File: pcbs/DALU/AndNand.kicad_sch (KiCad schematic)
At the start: 2 parts, among them U301 74HC00, U302 74HC00

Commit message: Trying to figure out the hierarchical buses
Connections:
- net NAND1: now reaches U301.6
- net RESULT0 renamed NAND0
- net RESULT2 renamed NAND2
- net RESULT3 renamed NAND3
- net RESULT4 renamed NAND4
- net RESULT5 renamed NAND5
- net RESULT6 renamed NAND6
- net RESULT7 renamed NAND7

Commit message: Trying to get everything together
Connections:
- net +5V: now reaches U302.14 (VCC)
- net +5V: now also U301.14 (VCC)
- net GND: now reaches U302.7 (GND)
- net GND: now also U301.7 (GND)
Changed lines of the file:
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@@
+    (stroke (width 0) (type default) (color 0 0 0 0))
+  )
+  (wire (pts (xy 25.4 190.5) (xy 25.4 193.04))
     (stroke (width 0) (type default) (color 0 0 0 0))
   )
@@
     (stroke (width 0) (type default) (color 0 0 0 0))
   )
+  (wire (pts (xy 25.4 162.56) (xy 25.4 165.1))
+    (stroke (width 0) (type default) (color 0 0 0 0))
+  )
   (bus (pts (xy 114.3 110.49) (xy 114.3 124.46))
     (stroke (width 0) (type default) (color 0 0 0 0))
@@
     (stroke (width 0) (type default) (color 0 0 0 0))
   )
+  (wire (pts (xy 53.34 190.5) (xy 53.34 193.04))
+    (stroke (width 0) (type default) (color 0 0 0 0))
+  )
   (bus (pts (xy 120.65 27.94) (xy 114.3 27.94))
     (stroke (width 0) (type default) (color 0 0 0 0))
@@
   )
   (bus (pts (xy 60.96 93.98) (xy 60.96 107.95))
+    (stroke (width 0) (type default) (color 0 0 0 0))
+  )
+  (wire (pts (xy 53.34 162.56) (xy 53.34 165.1))
     (stroke (width 0) (type default) (color 0 0 0 0))
   )
@@
   (hierarchical_label "A[0..7]" (shape input) (at 24.13 25.4 180)
     (effects (font (size 1.27 1.27)) (justify right))
+  )
+  (symbol (lib_id "power:+5V") (at 53.34 162.56 0) (unit 1)
+    (in_bom yes) (on_board yes) (fields_autoplaced)
+    (property "Reference" "#PWR0303" (id 0) (at 53.34 166.37 0)
+      (effects (font (size 1.27 1.27)) hide)
+    )
+    (property "Value" "+5V" (id 1) (at 53.34 157.48 0))
+    (property "Footprint" "" (id 2) (at 53.34 162.56 0)
+      (effects (font (size 1.27 1.27)) hide)
+    )
+    (property "Datasheet" "" (id 3) (at 53.34 162.56 0)
+      (effects (font (size 1.27 1.27)) hide)
+    )
+    (pin "1")
+  )
+  (symbol (lib_id "power:GND") (at 25.4 193.04 0) (unit 1)
+    (in_bom yes) (on_board yes) (fields_autoplaced)
+    (property "Reference" "#PWR0302" (id 0) (at 25.4 199.39 0)
+      (effects (font (size 1.27 1.27)) hide)
+    )
+    (property "Value" "GND" (id 1) (at 25.4 198.12 0))
+    (property "Footprint" "" (id 2) (at 25.4 193.04 0)
+      (effects (font (size 1.27 1.27)) hide)
+    )
+    (property "Datasheet" "" (id 3) (at 25.4 193.04 0)
+      (effects (font (size 1.27 1.27)) hide)
+    )
+    (pin "1")
   )
   (symbol (lib_id "74xx:74HC00") (at 83.82 113.03 0) (unit 2)
@@
     (pin "7")
   )
+  (symbol (lib_id "power:GND") (at 53.34 193.04 0) (unit 1)
+    (in_bom yes) (on_board yes) (fields_autoplaced)
+    (property "Reference" "#PWR0304" (id 0) (at 53.34 199.39 0)
+      (effects (font (size 1.27 1.27)) hide)
+    )
+    (property "Value" "GND" (id 1) (at 53.34 198.12 0))
+    (property "Footprint" "" (id 2) (at 53.34 193.04 0)
+      (effects (font (size 1.27 1.27)) hide)
+    )
+    (property "Datasheet" "" (id 3) (at 53.34 193.04 0)
+      (effects (font (size 1.27 1.27)) hide)
+    )
+    (pin "1")
+  )
   (symbol (lib_id "74xx:74HC00") (at 83.82 140.97 0) (unit 3)
     (in_bom yes) (on_board yes) (fields_autoplaced)
@@
     (pin "7")
   )
+  (symbol (lib_id "power:+5V") (at 25.4 162.56 0) (unit 1)
+    (in_bom yes) (on_board yes) (fields_autoplaced)
+    (property "Reference" "#PWR0301" (id 0) (at 25.4 166.37 0)
+      (effects (font (size 1.27 1.27)) hide)
+    )
+    (property "Value" "+5V" (id 1) (at 25.4 157.48 0))
+    (property "Footprint" "" (id 2) (at 25.4 162.56 0)
+      (effects (font (size 1.27 1.27)) hide)
+    )
+    (property "Datasheet" "" (id 3) (at 25.4 162.56 0)
+      (effects (font (size 1.27 1.27)) hide)
+    )
+    (pin "1")
+  )
   (symbol (lib_id "74xx:74HC00") (at 83.82 99.06 0) (unit 1)

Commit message: Rethinking some design
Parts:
- added U303: 74HCT541, Package_DIP:DIP-20_W7.62mm_Socket, symbol 74xx:74HCT541
- added U304: 74LS540, Package_DIP:DIP-20_W7.62mm_Socket, symbol 74xx:74LS540
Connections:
- net +5V: now also U303.20 (VCC), U304.20 (VCC)
- net GND: now also U303.10 (GND), U304.10 (GND)
- net NAND0: now also U303.2 (A0), U304.2 (A0)
- net NAND1: now also U303.3 (A1), U304.3 (A1)
- net NAND2: now also U303.4 (A2), U304.4 (A2)
- net NAND3: now also U303.5 (A3), U304.5 (A3)
- net NAND4: now also U303.6 (A4), U304.6 (A4)
- net NAND5: now also U303.7 (A5), U304.7 (A5)
- net NAND6: now also U303.8 (A6), U304.8 (A6)
- net NAND7: now also U303.9 (A7), U304.9 (A7)
- new net ~{ENABLE_{AND}}: U304.1 (G1), U304.19 (G2)
- new net ~{ENABLE_{NAND}}: U303.1 (G1), U303.19 (G2)

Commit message: Thinking about some of the control logic
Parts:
- U301, U302: footprint (none) -> Package_DIP:DIP-14_W7.62mm_Socket
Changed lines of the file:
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@@
     (property "Reference" "U302" (id 0) (at 83.82 104.14 0))
     (property "Value" "74HC00" (id 1) (at 83.82 106.68 0))
-    (property "Footprint" "" (id 2) (at 83.82 113.03 0)
+    (property "Footprint" "Package_DIP:DIP-14_W7.62mm_Socket" (id 2) (at 83.82 113.03 0)
       (effects (font (size 1.27 1.27)) hide)
     )
@@
     (property "Reference" "U301" (id 0) (at 83.82 62.23 0))
     (property "Value" "74HC00" (id 1) (at 83.82 64.77 0))
-    (property "Footprint" "" (id 2) (at 83.82 71.12 0)
+    (property "Footprint" "Package_DIP:DIP-14_W7.62mm_Socket" (id 2) (at 83.82 71.12 0)
       (effects (font (size 1.27 1.27)) hide)
     )
@@
     (property "Reference" "U302" (id 0) (at 83.82 132.08 0))
     (property "Value" "74HC00" (id 1) (at 83.82 134.62 0))
-    (property "Footprint" "" (id 2) (at 83.82 140.97 0)
+    (property "Footprint" "Package_DIP:DIP-14_W7.62mm_Socket" (id 2) (at 83.82 140.97 0)
       (effects (font (size 1.27 1.27)) hide)
     )
@@
     (property "Reference" "U301" (id 0) (at 83.82 76.2 0))
     (property "Value" "74HC00" (id 1) (at 83.82 78.74 0))
-    (property "Footprint" "" (id 2) (at 83.82 85.09 0)
+    (property "Footprint" "Package_DIP:DIP-14_W7.62mm_Socket" (id 2) (at 83.82 85.09 0)
       (effects (font (size 1.27 1.27)) hide)
     )
@@
     (property "Reference" "U302" (id 0) (at 83.82 118.11 0))
     (property "Value" "74HC00" (id 1) (at 83.82 120.65 0))
-    (property "Footprint" "" (id 2) (at 83.82 127 0)
+    (property "Footprint" "Package_DIP:DIP-14_W7.62mm_Socket" (id 2) (at 83.82 127 0)
       (effects (font (size 1.27 1.27)) hide)
     )
@@
     (property "Reference" "U301" (id 0) (at 83.82 48.26 0))
     (property "Value" "74HC00" (id 1) (at 83.82 50.8 0))
-    (property "Footprint" "" (id 2) (at 83.82 57.15 0)
+    (property "Footprint" "Package_DIP:DIP-14_W7.62mm_Socket" (id 2) (at 83.82 57.15 0)
       (effects (font (size 1.27 1.27)) hide)
     )
@@
       (effects (font (size 1.27 1.27)) (justify left))
     )
-    (property "Footprint" "" (id 2) (at 53.34 177.8 0)
+    (property "Footprint" "Package_DIP:DIP-14_W7.62mm_Socket" (id 2) (at 53.34 177.8 0)
       (effects (font (size 1.27 1.27)) hide)
     )
@@
       (effects (font (size 1.27 1.27)) (justify left))
     )
-    (property "Footprint" "" (id 2) (at 25.4 177.8 0)
-      (effects (font (size 1.27 1.27)) hide)
-    )
+    (property "Footprint" "Package_DIP:DIP-14_W7.62mm_Socket" (id 2) (at 25.4 177.8 0)
+      (effects (font (size 1.27 1.27)) hide)
+    )

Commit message: Doing some rethinking
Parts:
- removed U303: 74HCT541, Package_DIP:DIP-20_W7.62mm_Socket, symbol 74xx:74HCT541
- removed U304: 74LS540, Package_DIP:DIP-20_W7.62mm_Socket, symbol 74xx:74LS540
- added U403, U404: 74HC245, Package_SO:SOIC-20W_7.5x12.8mm_P1.27mm, symbol 74xx:74HC245
- renumbered U301 to U401, U302 to U402
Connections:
- net +5V: now also U403.20 (VCC), U404.20 (VCC)
- net GND: now also U403.10 (GND), U404.10 (GND)
- net NAND0: now also U403.2 (A0)
- net NAND1: now also U403.3 (A1)
- net NAND2: now also U403.4 (A2)
- net NAND3: now also U403.5 (A3)
- net NAND4: now also U403.6 (A4)
- net NAND5: now also U403.7 (A5)
- net NAND6: now also U403.8 (A6)
- net NAND7: now also U403.9 (A7)

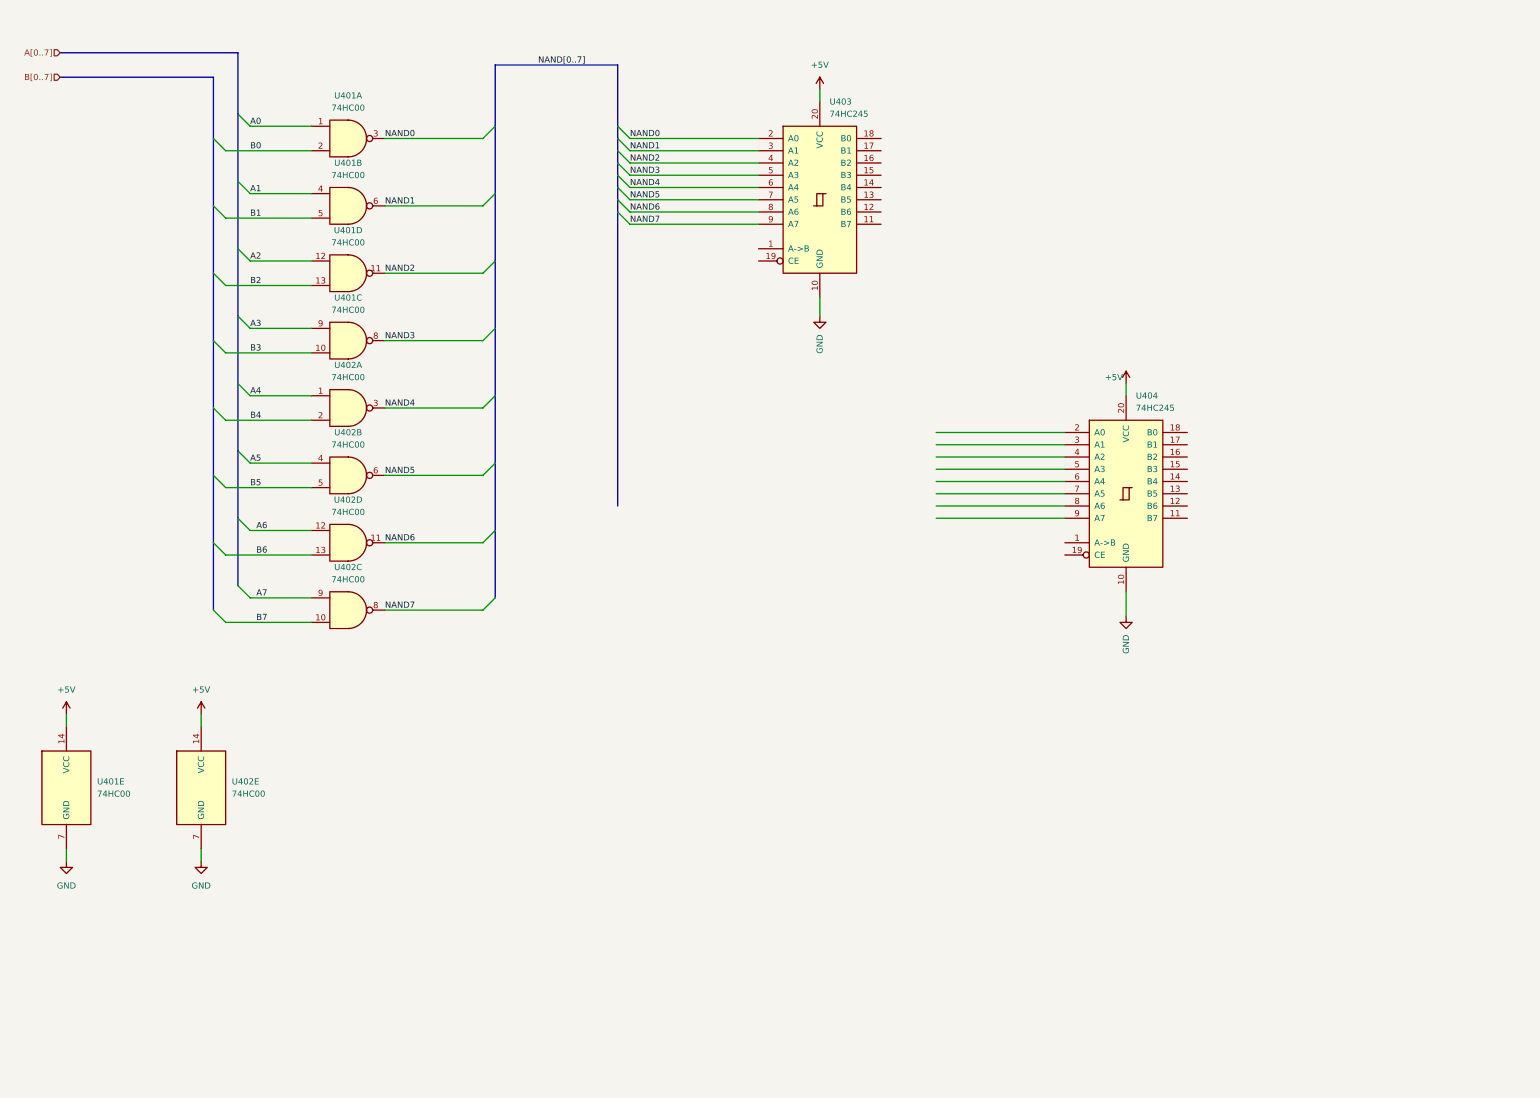
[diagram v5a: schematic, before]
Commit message: Input stage fiddling
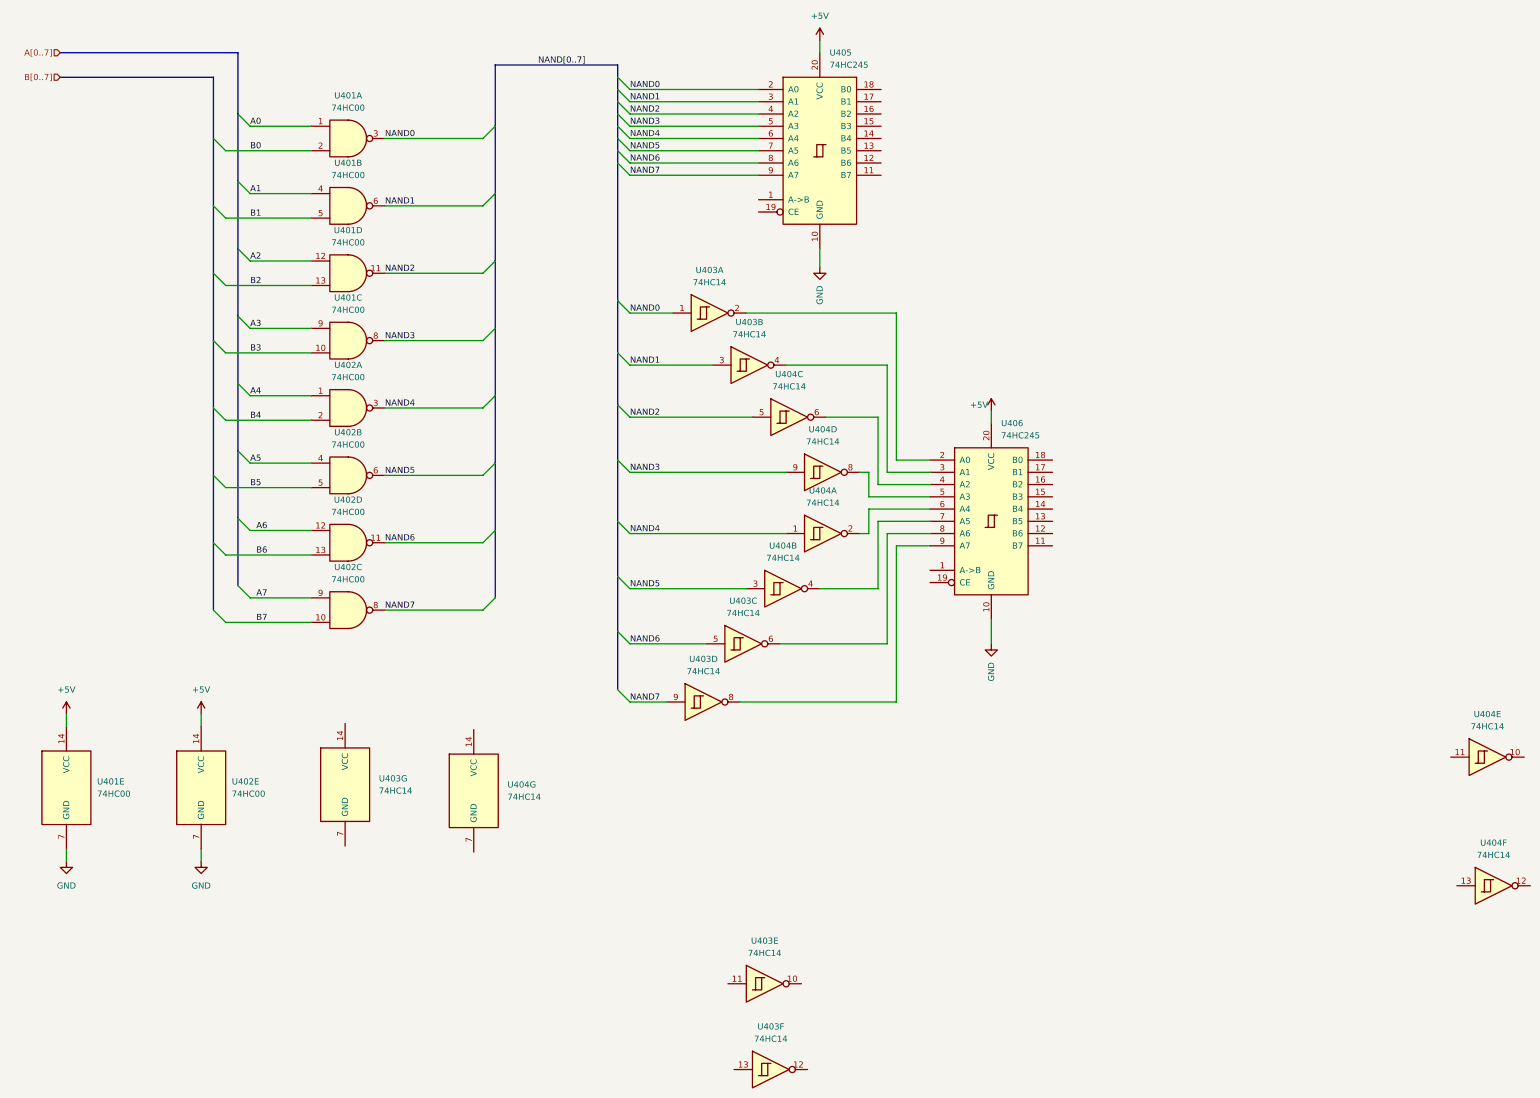
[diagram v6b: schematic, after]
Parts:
- added U403, U404: 74HC14, Package_SO:SOIC-14_3.9x8.7mm_P1.27mm, symbol 74xx:74HC14
- renumbered U403 to U405, U404 to U406
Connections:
- net NAND0: now also U403.1
- net NAND1: now also U403.3
- net NAND2: now also U404.5
- net NAND3: now also U404.9
- net NAND4: now also U404.1
- net NAND5: now also U404.3
- net NAND6: now also U403.5
- net NAND7: now also U403.9
- net at U406.2 (A0): now also U403.2
- net at U406.3 (A1): now also U403.4
- net at U406.4 (A2): now also U404.6
- net at U406.5 (A3): now also U404.8
- net at U406.6 (A4): now also U404.2
- net at U406.7 (A5): now also U404.4
- net at U406.8 (A6): now also U403.6
- net at U406.9 (A7): now also U403.8
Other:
- moved on the sheet: U405, U406

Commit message: Starting to think about decoding etc.
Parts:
- renumbered U401 to U501, U402 to U502, U403 to U503, U404 to U504, U405 to U505, U406 to U506
